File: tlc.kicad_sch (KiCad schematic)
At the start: 13 parts, among them U5 TL074, U6 TL074, U7 TLC7528

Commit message: reworking with Pot Lights
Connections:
- net +12V: now also U5.4 (V+), U6.4 (V+); no longer U5.11 (V-), U6.11 (V-)
- net -12V: now also U5.11 (V-), U6.11 (V-); no longer U5.4 (V+), U6.4 (V+)
- net -1V65: now also U5.10 (+), U6.10 (+); no longer U5.3 (+), U6.3 (+)
- net GND: now also U5.12 (+), U5.3 (+), U5.5 (+), U6.12 (+), U6.3 (+), U6.5 (+); no longer U5.10 (+), U5.12 (+), U5.5 (+), U6.10 (+), U6.12 (+), U6.5 (+)
- net OutA: now also U5.1; no longer U5.8
- net OutB: now also U6.1; no longer U6.8
- net at R5.2, R7.1: now also U5.9 (-); no longer U5.2 (-)
- net at R6.2, R8.1: now also U6.9 (-); no longer U6.2 (-)
- net at R8.2, U7.18 (REFB): now also U6.8; no longer U6.1
- net at C8.2, R10.1, U7.19 (RFBB): now also U6.14; no longer U6.7
- net at R10.2, R12.1: now also U6.2 (-); no longer U6.9 (-)
- net at R7.2, U7.4 (REFA): now also U5.8; no longer U5.1
- net at C9.1, R9.1, U7.3 (RFBA): now also U5.14; no longer U5.7
- net at R11.1, R9.2: now also U5.2 (-); no longer U5.9 (-)
- net at C9.2, U7.2 (OUTA): now also U5.13 (-); no longer U5.6 (-)
- net at C8.1, U7.20 (OUTB): now also U6.13 (-); no longer U6.6 (-)
- new net: U6.6 (-), U6.7
- new net: U5.6 (-), U5.7
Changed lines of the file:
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@@
     (pin "1")
   )
-  (symbol (lib_id "eurorack:TL074") (at 236.22 139.065 0) (mirror x) (unit 4)
+  (symbol (lib_id "eurorack:TL074") (at 236.22 139.065 0) (mirror x) (unit 2)
     (in_bom yes) (on_board yes)
     (property "Reference" "U6" (id 0) (at 238.76 142.875 0))
@@
     (pin "1")
   )
-  (symbol (lib_id "eurorack:TL074") (at 267.97 30.48 0) (mirror x) (unit 5)
-    (in_bom yes) (on_board yes)
-    (property "Reference" "U6" (id 0) (at 270.51 34.29 0))
-    (property "Value" "TL074" (id 1) (at 266.7 30.48 0))
-    (property "Footprint" "Package_SO:SO-14_5.3x10.2mm_P1.27mm" (id 2) (at 266.7 33.02 0)
-      (effects (font (size 1.27 1.27)) hide)
-    )
-    (property "Datasheet" "https://cdn-reichelt.de/documents/datenblatt/A200/TL074%23STM.pdf" (id 3) (at 269.24 35.56 0)
+  (symbol (lib_id "eurorack:TL074") (at 262.89 30.48 0) (mirror y) (unit 5)
+    (in_bom yes) (on_board yes)
+    (property "Reference" "U6" (id 0) (at 260.35 26.67 0))
+    (property "Value" "TL074" (id 1) (at 264.16 30.48 0))
+    (property "Footprint" "Package_SO:SO-14_5.3x10.2mm_P1.27mm" (id 2) (at 264.16 27.94 0)
+      (effects (font (size 1.27 1.27)) hide)
+    )
+    (property "Datasheet" "https://cdn-reichelt.de/documents/datenblatt/A200/TL074%23STM.pdf" (id 3) (at 261.62 25.4 0)
       (effects (font (size 1.27 1.27)) hide)
     )
@@
     (pin "1")
   )
-  (symbol (lib_id "eurorack:TL074") (at 255.27 30.48 0) (mirror x) (unit 5)
-    (in_bom yes) (on_board yes)
-    (property "Reference" "U5" (id 0) (at 257.81 34.29 0))
-    (property "Value" "TL074" (id 1) (at 254 30.48 0))
-    (property "Footprint" "Package_SO:SO-14_5.3x10.2mm_P1.27mm" (id 2) (at 254 33.02 0)
-      (effects (font (size 1.27 1.27)) hide)
-    )
-    (property "Datasheet" "https://cdn-reichelt.de/documents/datenblatt/A200/TL074%23STM.pdf" (id 3) (at 256.54 35.56 0)
+  (symbol (lib_id "eurorack:TL074") (at 250.19 30.48 0) (mirror y) (unit 5)
+    (in_bom yes) (on_board yes)
+    (property "Reference" "U5" (id 0) (at 247.65 26.67 0))
+    (property "Value" "TL074" (id 1) (at 251.46 30.48 0))
+    (property "Footprint" "Package_SO:SO-14_5.3x10.2mm_P1.27mm" (id 2) (at 251.46 27.94 0)
+      (effects (font (size 1.27 1.27)) hide)
+    )
+    (property "Datasheet" "https://cdn-reichelt.de/documents/datenblatt/A200/TL074%23STM.pdf" (id 3) (at 248.92 25.4 0)
       (effects (font (size 1.27 1.27)) hide)
     )
@@
     (pin "2")
   )
-  (symbol (lib_id "eurorack:TL074") (at 86.36 35.56 0) (mirror x) (unit 1)
+  (symbol (lib_id "eurorack:TL074") (at 86.36 35.56 0) (mirror x) (unit 3)
     (in_bom yes) (on_board yes)
     (property "Reference" "U5" (id 0) (at 87.63 39.37 0))
@@
     (pin "2")
   )
-  (symbol (lib_id "eurorack:TL074") (at 210.82 101.6 0) (mirror x) (unit 3)
+  (symbol (lib_id "eurorack:TL074") (at 210.82 101.6 0) (mirror x) (unit 1)
     (in_bom yes) (on_board yes)
     (property "Reference" "U6" (id 0) (at 213.36 105.41 0))
@@
     (pin "2")
   )
-  (symbol (lib_id "eurorack:TL074") (at 170.18 99.06 0) (mirror x) (unit 2)
+  (symbol (lib_id "eurorack:TL074") (at 170.18 99.06 0) (mirror x) (unit 4)
     (in_bom yes) (on_board yes)
     (property "Reference" "U6" (id 0) (at 171.45 102.87 0))
@@
     (pin "4")
   )
-  (symbol (lib_id "eurorack:TL074") (at 214.63 139.065 0) (mirror x) (unit 4)
+  (symbol (lib_id "eurorack:TL074") (at 214.63 139.065 0) (mirror x) (unit 2)
     (in_bom yes) (on_board yes)
     (property "Reference" "U5" (id 0) (at 217.17 142.875 0))
@@
     (pin "2")
   )
-  (symbol (lib_id "eurorack:TL074") (at 86.36 147.32 0) (mirror x) (unit 1)
+  (symbol (lib_id "eurorack:TL074") (at 86.36 147.32 0) (mirror x) (unit 3)
     (in_bom yes) (on_board yes)
     (property "Reference" "U6" (id 0) (at 87.63 151.13 0))
@@
     (pin "1")
   )
-  (symbol (lib_id "eurorack:TL074") (at 170.18 81.28 0) (mirror x) (unit 2)
+  (symbol (lib_id "eurorack:TL074") (at 170.18 81.28 0) (mirror x) (unit 4)
     (in_bom yes) (on_board yes)
     (property "Reference" "U5" (id 0) (at 171.45 85.09 0))
@@
     (pin "1")
   )
-  (symbol (lib_id "eurorack:TL074") (at 210.82 83.82 0) (mirror x) (unit 3)
+  (symbol (lib_id "eurorack:TL074") (at 210.82 83.82 0) (mirror x) (unit 1)
     (in_bom yes) (on_board yes)
     (property "Reference" "U5" (id 0) (at 213.36 87.63 0))

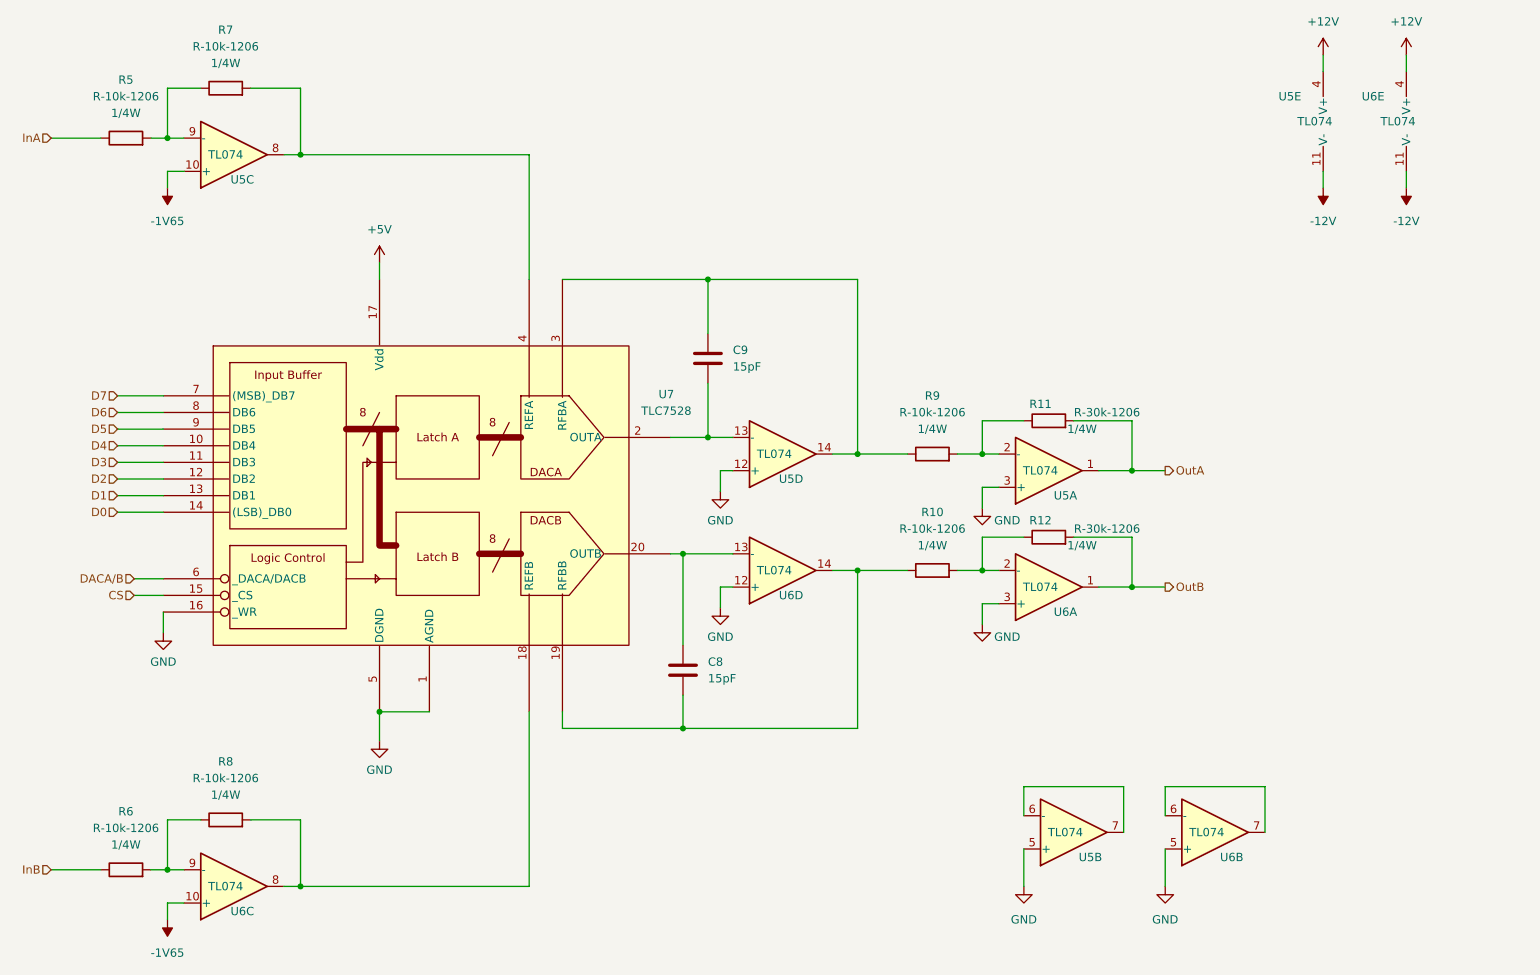
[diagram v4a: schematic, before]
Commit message: fixed issues, power still needs to be addressed
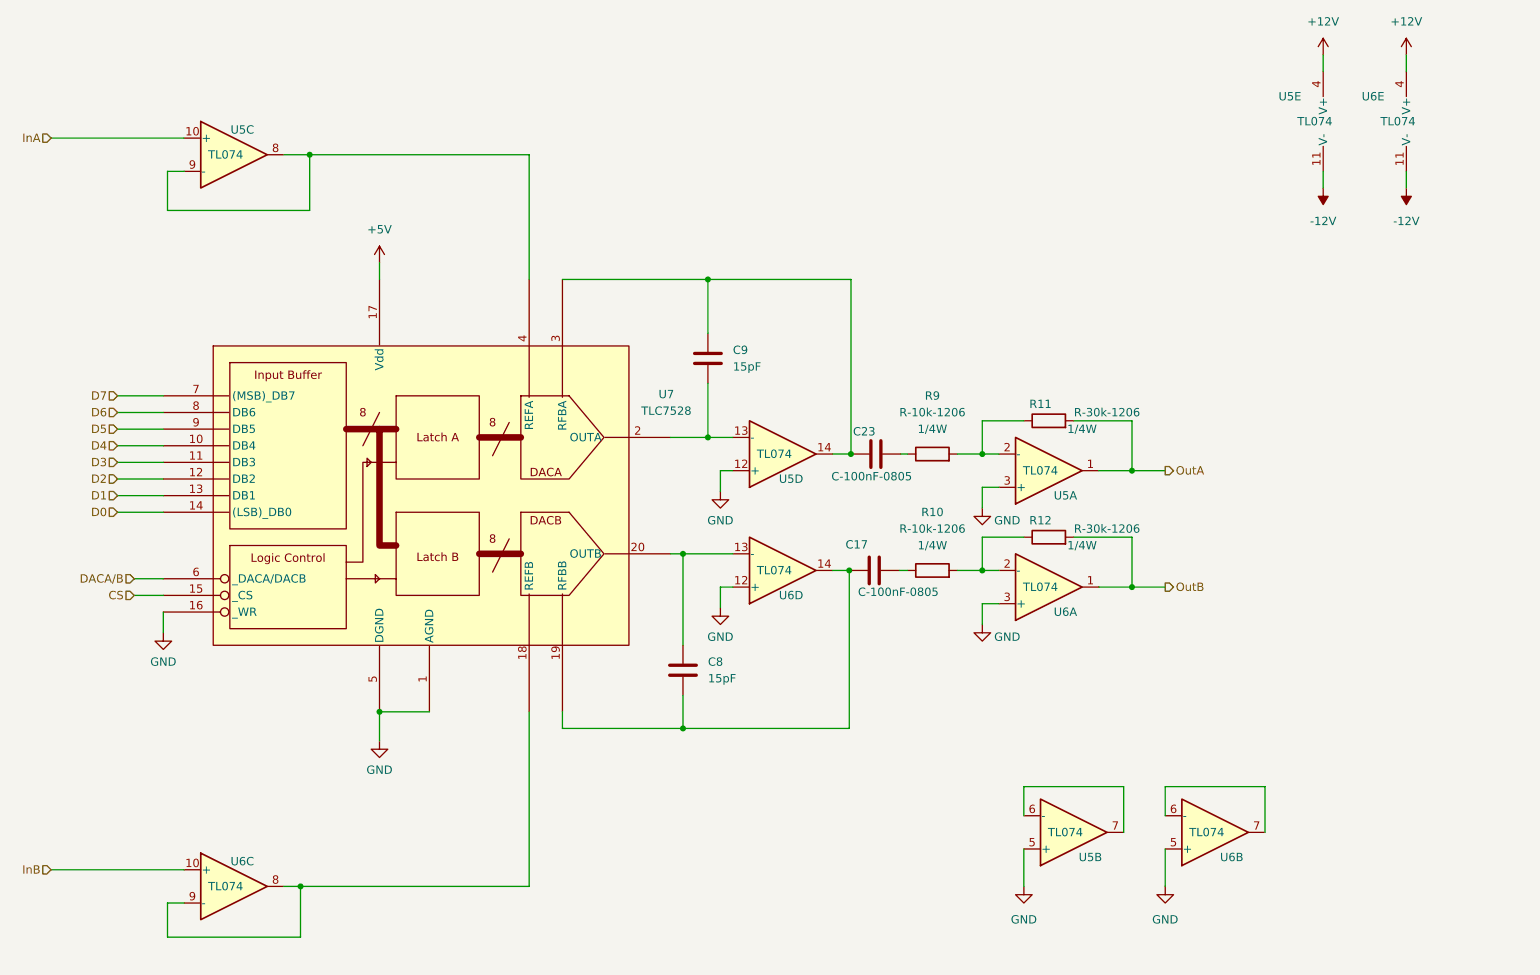
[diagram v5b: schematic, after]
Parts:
- removed R5, R6, R7, R8: R-10k-1206, Resistor_SMD:R_1206_3216Metric_Pad1.30x1.75mm_HandSolder, symbol eurorack:R-10k-1206
- added C17, C23: C-100nF-0805, Capacitor_SMD:C_0805_2012Metric_Pad1.18x1.45mm_HandSolder, symbol eurorack:C-100nF-0805
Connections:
- net InA: now also U5.10 (+)
- net InB: now also U6.10 (+)
- net at U5.9 (-): now also U5.8, U7.4 (REFA)
- net at U6.9 (-): now also U6.8, U7.18 (REFB)
- net at C8.2, U6.14, U7.19 (RFBB): now also C17.1; no longer R10.1
- net at C9.1, U5.14, U7.3 (RFBA): now also C23.1; no longer R9.1
- removed net -1V65: U5.10 (+), U6.10 (+)
- new net: C17.2, R10.1
- new net: C23.2, R9.1

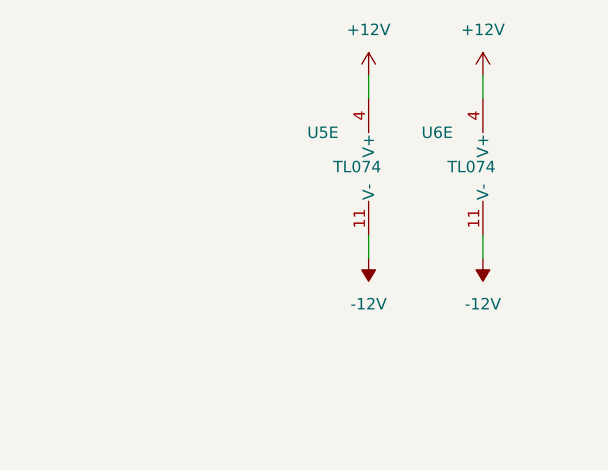
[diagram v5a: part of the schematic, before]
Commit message: working on lifted leds
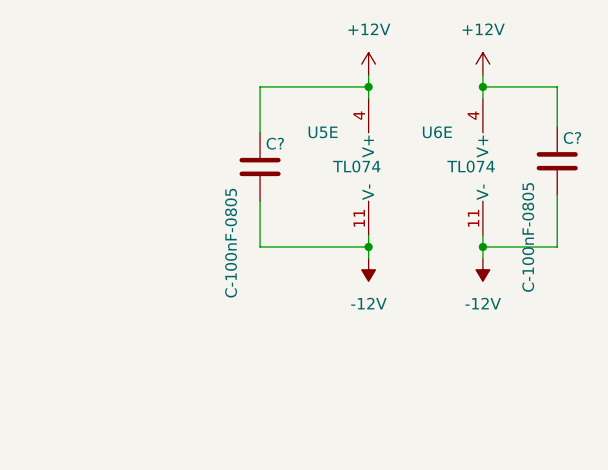
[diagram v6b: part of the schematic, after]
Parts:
- added C? (x2): C-100nF-0805, Capacitor_SMD:C_0805_2012Metric_Pad1.18x1.45mm_HandSolder, symbol eurorack:C-100nF-0805
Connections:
- net +12V: now also C?.1, C?.1
- net -12V: now also C?.2, C?.2
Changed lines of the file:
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@@
   (junction (at 158.75 54.61) (diameter 0) (color 0 0 0 0)
   )
+  (junction (at 252.73 21.59) (diameter 0) (color 0 0 0 0)
+  )
+  (junction (at 252.73 39.37) (diameter 0) (color 0 0 0 0)
+  )
   (junction (at 108.585 120.65) (diameter 0) (color 0 0 0 0)
   )
   (junction (at 180.34 99.06) (diameter 0) (color 0 0 0 0)
   )
+  (junction (at 265.43 39.37) (diameter 0) (color 0 0 0 0)
+  )
   (junction (at 200.66 99.06) (diameter 0) (color 0 0 0 0)
   )
@@
   (junction (at 223.52 101.6) (diameter 0) (color 0 0 0 0)
   )
+  (junction (at 265.43 21.59) (diameter 0) (color 0 0 0 0)
+  )
   (junction (at 154.94 123.19) (diameter 0) (color 0 0 0 0)
   )
@@
     (stroke (width 0) (type default) (color 0 0 0 0))
   )
+  (wire (pts (xy 252.73 21.59) (xy 252.73 22.86))
+    (stroke (width 0) (type default) (color 0 0 0 0))
+  )
   (wire (pts (xy 153.035 78.74) (xy 158.75 78.74))
     (stroke (width 0) (type default) (color 0 0 0 0))
   )
-  (wire (pts (xy 252.73 38.1) (xy 252.73 40.64))
+  (wire (pts (xy 252.73 38.1) (xy 252.73 39.37))
     (stroke (width 0) (type default) (color 0 0 0 0))
   )
@@
     (stroke (width 0) (type default) (color 0 0 0 0))
   )
+  (wire (pts (xy 265.43 39.37) (xy 265.43 40.64))
+    (stroke (width 0) (type default) (color 0 0 0 0))
+  )
   (wire (pts (xy 228.6 141.605) (xy 228.6 147.32))
     (stroke (width 0) (type default) (color 0 0 0 0))
@@
     (stroke (width 0) (type default) (color 0 0 0 0))
   )
-  (wire (pts (xy 252.73 20.32) (xy 252.73 22.86))
+  (wire (pts (xy 252.73 20.32) (xy 252.73 21.59))
     (stroke (width 0) (type default) (color 0 0 0 0))
   )
@@
     (stroke (width 0) (type default) (color 0 0 0 0))
   )
+  (wire (pts (xy 273.685 39.37) (xy 265.43 39.37))
+    (stroke (width 0) (type default) (color 0 0 0 0))
+  )
   (wire (pts (xy 200.66 99.06) (xy 203.2 99.06))
     (stroke (width 0) (type default) (color 0 0 0 0))
@@
     (stroke (width 0) (type default) (color 0 0 0 0))
   )
+  (wire (pts (xy 273.685 21.59) (xy 273.685 26.035))
+    (stroke (width 0) (type default) (color 0 0 0 0))
+  )
   (wire (pts (xy 180.594 54.61) (xy 180.594 81.28))
     (stroke (width 0) (type default) (color 0 0 0 0))
@@
     (stroke (width 0) (type default) (color 0 0 0 0))
   )
-  (wire (pts (xy 265.43 38.1) (xy 265.43 40.64))
+  (wire (pts (xy 265.43 38.1) (xy 265.43 39.37))
+    (stroke (width 0) (type default) (color 0 0 0 0))
+  )
+  (wire (pts (xy 252.73 39.37) (xy 252.73 40.64))
     (stroke (width 0) (type default) (color 0 0 0 0))
   )
@@
     (stroke (width 0) (type default) (color 0 0 0 0))
   )
+  (wire (pts (xy 240.665 34.29) (xy 240.665 39.37))
+    (stroke (width 0) (type default) (color 0 0 0 0))
+  )
   (wire (pts (xy 158.75 54.61) (xy 158.75 62.865))
     (stroke (width 0) (type default) (color 0 0 0 0))
@@
     (stroke (width 0) (type default) (color 0 0 0 0))
   )
+  (wire (pts (xy 265.43 21.59) (xy 265.43 22.86))
+    (stroke (width 0) (type default) (color 0 0 0 0))
+  )
   (wire (pts (xy 78.74 38.1) (xy 76.2 38.1))
     (stroke (width 0) (type default) (color 0 0 0 0))
@@
     (stroke (width 0) (type default) (color 0 0 0 0))
   )
+  (wire (pts (xy 240.665 26.67) (xy 240.665 21.59))
+    (stroke (width 0) (type default) (color 0 0 0 0))
+  )
   (wire (pts (xy 154.94 96.52) (xy 154.94 110.49))
     (stroke (width 0) (type default) (color 0 0 0 0))
@@
     (stroke (width 0) (type default) (color 0 0 0 0))
   )
+  (wire (pts (xy 240.665 21.59) (xy 252.73 21.59))
+    (stroke (width 0) (type default) (color 0 0 0 0))
+  )
   (wire (pts (xy 96.52 155.067) (xy 96.52 147.32))
     (stroke (width 0) (type default) (color 0 0 0 0))
@@
     (stroke (width 0) (type default) (color 0 0 0 0))
   )
+  (wire (pts (xy 265.43 21.59) (xy 273.685 21.59))
+    (stroke (width 0) (type default) (color 0 0 0 0))
+  )
   (wire (pts (xy 200.66 86.36) (xy 200.66 89.535))
     (stroke (width 0) (type default) (color 0 0 0 0))
   )
+  (wire (pts (xy 240.665 39.37) (xy 252.73 39.37))
+    (stroke (width 0) (type default) (color 0 0 0 0))
+  )
   (wire (pts (xy 158.75 54.61) (xy 180.594 54.61))
     (stroke (width 0) (type default) (color 0 0 0 0))
@@
     (stroke (width 0) (type default) (color 0 0 0 0))
   )
+  (wire (pts (xy 273.685 33.655) (xy 273.685 39.37))
+    (stroke (width 0) (type default) (color 0 0 0 0))
+  )
   (wire (pts (xy 131.445 120.65) (xy 131.445 147.32))
     (stroke (width 0) (type default) (color 0 0 0 0))
@@
     (stroke (width 0) (type default) (color 0 0 0 0))
   )
-  (wire (pts (xy 265.43 20.32) (xy 265.43 22.86))
+  (wire (pts (xy 265.43 20.32) (xy 265.43 21.59))
     (stroke (width 0) (type default) (color 0 0 0 0))
   )
@@
   (hierarchical_label "D2" (shape input) (at 68.58 85.09 180)
     (effects (font (size 1.27 1.27)) (justify right))
+  )
+  (symbol (lib_id "eurorack:C-100nF-0805") (at 273.685 29.845 0) (unit 1)
+    (in_bom yes) (on_board yes)
+    (property "Reference" "C?" (id 0) (at 274.32 27.305 0)
+      (effects (font (size 1.27 1.27)) (justify left))
+    )
+    (property "Value" "C-100nF-0805" (id 1) (at 270.51 44.45 90)
+      (effects (font (size 1.27 1.27)) (justify left))
+    )
+    (property "Footprint" "Capacitor_SMD:C_0805_2012Metric_Pad1.18x1.45mm_HandSolder" (id 2) (at 274.6502 33.655 0)
+      (effects (font (size 1.27 1.27)) hide)
+    )
+    (property "Datasheet" "https://secure.reichelt.com/at/en/smd-multilayer-ceramic-capacitor-100-n-10--x7r-g0805-100n-p31879.html?&nbc=1" (id 3) (at 273.685 29.845 0)
+      (effects (font (size 1.27 1.27)) hide)
+    )
+    (pin "1")
+    (pin "2")
   )
   (symbol (lib_id "power:GND") (at 228.6 147.32 0) (unit 1)
@@
     (pin "4")
   )
+  (symbol (lib_id "eurorack:C-100nF-0805") (at 240.665 30.48 0) (unit 1)
+    (in_bom yes) (on_board yes)
+    (property "Reference" "C?" (id 0) (at 241.3 27.94 0)
+      (effects (font (size 1.27 1.27)) (justify left))
+    )
+    (property "Value" "C-100nF-0805" (id 1) (at 237.49 45.085 90)
+      (effects (font (size 1.27 1.27)) (justify left))
+    )
+    (property "Footprint" "Capacitor_SMD:C_0805_2012Metric_Pad1.18x1.45mm_HandSolder" (id 2) (at 241.6302 34.29 0)
+      (effects (font (size 1.27 1.27)) hide)
+    )
+    (property "Datasheet" "https://secure.reichelt.com/at/en/smd-multilayer-ceramic-capacitor-100-n-10--x7r-g0805-100n-p31879.html?&nbc=1" (id 3) (at 240.665 30.48 0)
+      (effects (font (size 1.27 1.27)) hide)
+    )
+    (pin "1")
+    (pin "2")
+  )
   (symbol (lib_id "power:GND") (at 160.655 104.775 0) (unit 1)

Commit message: wip led panel
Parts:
- gave numbers to parts that had none: 2
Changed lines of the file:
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@@
   (symbol (lib_id "eurorack:C-100nF-0805") (at 273.685 29.845 0) (unit 1)
     (in_bom yes) (on_board yes)
-    (property "Reference" "C?" (id 0) (at 274.32 27.305 0)
+    (property "Reference" "C27" (id 0) (at 274.32 27.305 0)
       (effects (font (size 1.27 1.27)) (justify left))
     )
@@
   (symbol (lib_id "eurorack:C-100nF-0805") (at 240.665 30.48 0) (unit 1)
     (in_bom yes) (on_board yes)
-    (property "Reference" "C?" (id 0) (at 241.3 27.94 0)
+    (property "Reference" "C26" (id 0) (at 241.3 27.94 0)
       (effects (font (size 1.27 1.27)) (justify left))
     )
